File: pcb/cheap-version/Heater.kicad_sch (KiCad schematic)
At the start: 8 parts, among them J601 PTC + / switched - (3.5 mm), Q601 NTMFS5C628NLT1G, U601 UCC27524ADR

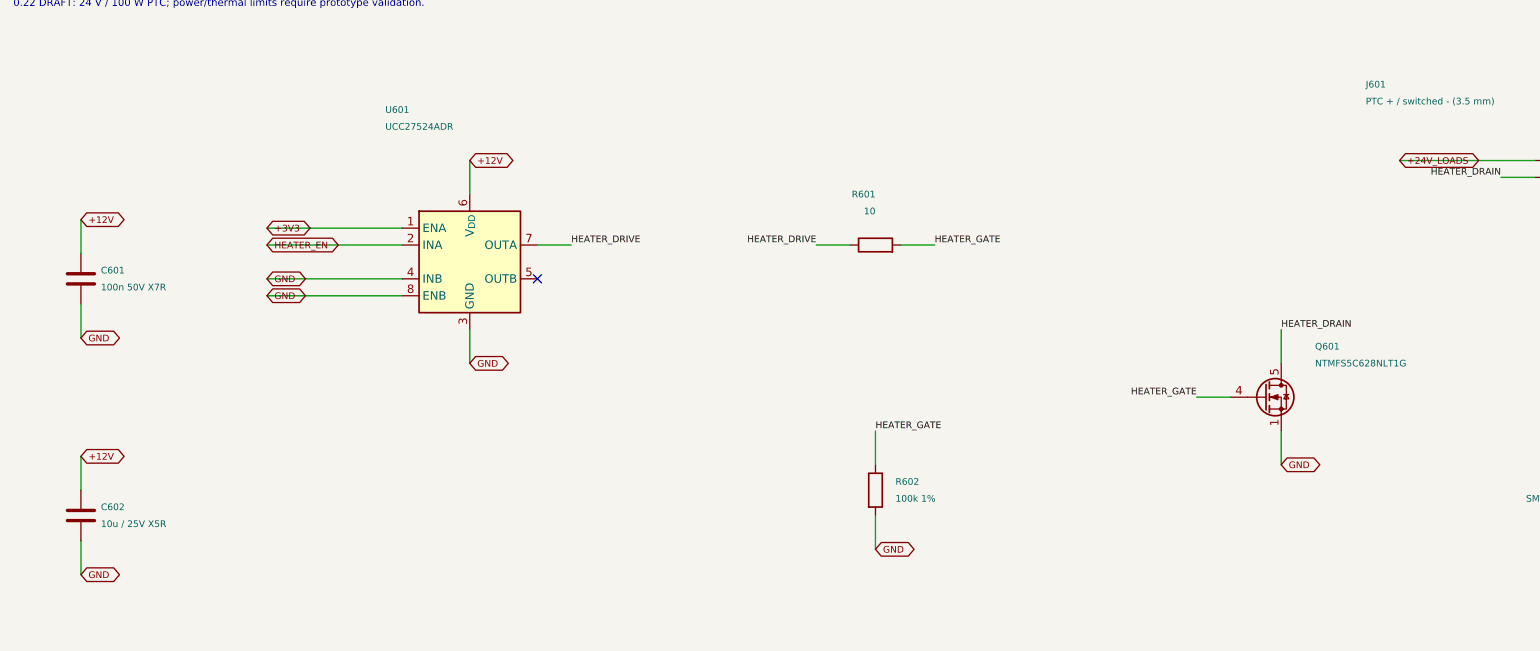
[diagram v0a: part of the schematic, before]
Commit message: cheap-version: schematic substitutions from stock parts
tools/make_cheap1.py generates the cheap-1 sheets from the PCB_V1 0.22 baseline:
ST1S14 for LMR16020 (RT resistor removed, EN/FB divider recalculated), IRS4427S and
IRL2505 for the heater, BSC146N10LS5 for the LED boost switches, SS56 diodes,
KF301/FS1.5/KF2510/XH connectors, stock resistors and capacitors (Source field =
stock:<id>). J901 XT60 is replaced by a screw terminal as decided. U101 TPS54202 and
D711/D721 SS5P10 are kept because datasheets for ST1S10 and SBRT15U100SP5 were not
available. ERC: 0 errors (one warning: footprint for the DTMSS-27 inductor pending);
netdiff against PCB_V1: no connectivity differences among untouched pins.

Co-Authored-By: Claude Sonnet 5.5 <noreply@anthropic.com>
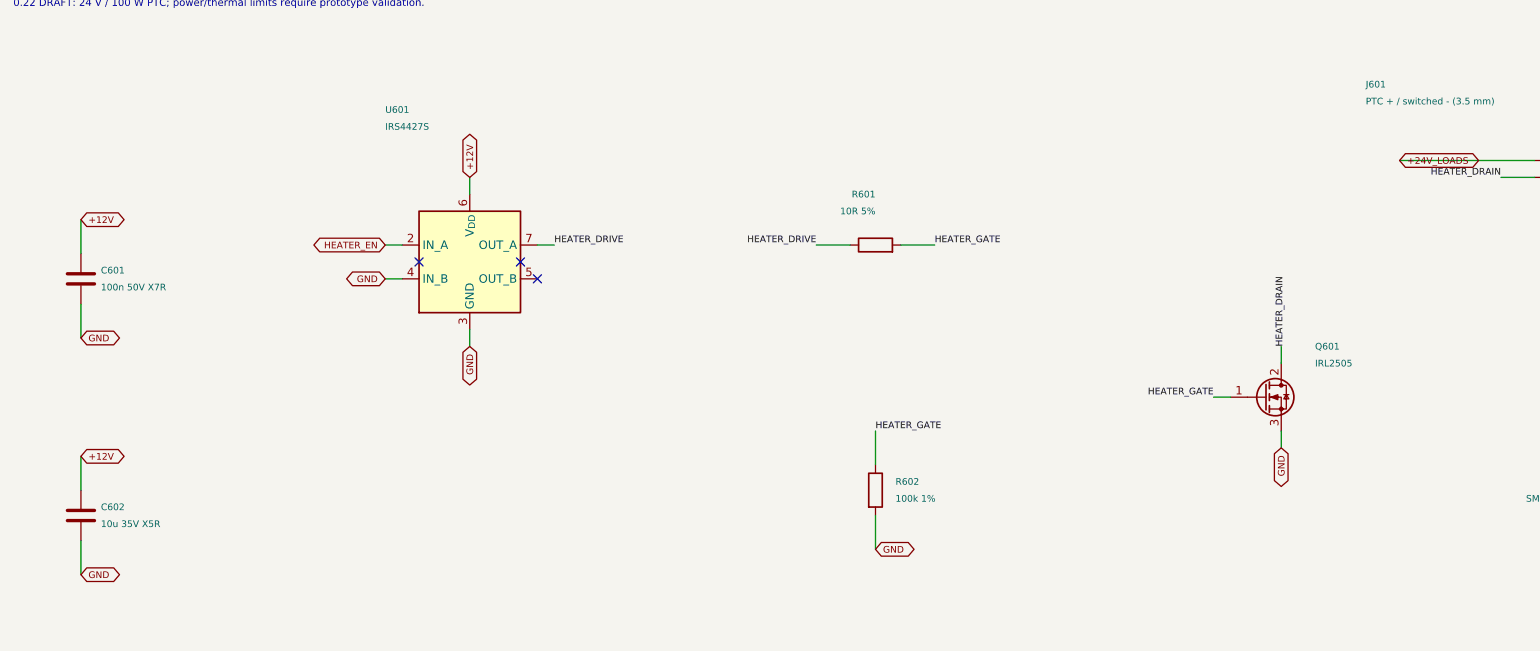
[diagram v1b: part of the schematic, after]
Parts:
- removed Q601: NTMFS5C628NLT1G, Package_SO:ONSemi_SO-8FL_488AA, symbol GrowBox:NTMFS5C628NL
- removed U601: UCC27524ADR, Package_SO:SOIC-8_3.9x4.9mm_P1.27mm, symbol Driver_FET:UCC27524D
- added Q601: IRL2505, Package_TO_SOT_THT:TO-220-3_Vertical, symbol Transistor_FET:Q_NMOS_GDS
- added U601: IRS4427S, Package_SO:SOIC-8_3.9x4.9mm_P1.27mm, symbol Driver_FET:TC4427xOA
- C601: Source (none) -> stock:54
- C602: value 10u / 25V X5R -> 10u 35V X5R; footprint Capacitor_SMD:C_0805_2012Metric -> Capacitor_SMD:C_1210_3225Metric; LCSC C15850 -> C2980162; MPN CL21A106KAYNNNE -> CL32A106KLULNNE; Source (none) -> stock:6
- J601: footprint GrowBox:TerminalBlock_DORABO_DB125-3.5_1x02_P3.50mm_Horizontal -> TerminalBlock_Phoenix:TerminalBlock_Phoenix_PT-1,5-2-3.5-H_1x02_P3.50mm_Horizontal; LCSC C466970 -> (none); MPN DB125-3.5-2P-GN-S -> FS1.5-02-350-2601R; Manufacturer DORABO -> (none); Source (none) -> stock:86
- R601: value 10 -> 10R 5%; footprint Resistor_SMD:R_0603_1608Metric -> Resistor_SMD:R_1206_3216Metric; Source (none) -> stock:41
- R602: LCSC C25803 -> C14675; MPN 0603WAF1003T5E -> RC0603FR-07100KL; Manufacturer UNI-ROYAL -> Yageo; Source (none) -> stock:55
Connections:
- net +12V: now also U601.6 (V_{DD})
- net GND: now also Q601.3 (S), U601.3 (GND), U601.4 (IN_B)
- net HEATER_DRAIN: now also Q601.2 (D)
- net HEATER_DRIVE: now also U601.7 (OUT_A)
- net HEATER_EN: now also U601.2 (IN_A)
- net HEATER_GATE: now also Q601.1 (G)
- no-connect marks 1 -> 3

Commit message: cheap-version: CH1 for 80 W and UCC27524 heater driver
R716 0.18 -> 0.12 ohm (1.667 A, 80 W at 48 V; the LED panel is rated up to
120 W and is not fully loaded). analyze_led_cheap.py re-run: input current
up to 4.61 A, inductor peak 6.26 A, OCP headroom 2.06 A, all model checks
pass; about 96 W is the ceiling of this controller/inductor pair.

U601 is the PCB_V1 UCC27524ADR again instead of the IRS4427S (2.5 V input
threshold left 0.14 V of margin at ESP32 VOH): ENA tied to +12V, ENB to
GND. Board side in tools/swap_heater_driver.py; generator, BOM and BUY
lists follow (order estimate USD 34.69). Schematic ERC 0, schematic and
board match pin by pin.

Co-Authored-By: Claude Sonnet 5.5 <noreply@anthropic.com>
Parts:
- U601: value IRS4427S -> UCC27524ADR; symbol Driver_FET:TC4427xOA -> Driver_FET:UCC27524D; LCSC (none) -> C185857; MPN IRS4427STRPBF -> UCC27524ADR; Manufacturer Infineon -> TI; Source stock:11 -> buy
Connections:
- net +12V: now also U601.1 (ENA)
- net GND: now also U601.8 (ENB)
- no-connect marks 3 -> 1
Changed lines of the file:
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@@
 	)
 	(symbol
-		(lib_id "Driver_FET:TC4427xOA")
+		(lib_id "Driver_FET:UCC27524D")
 		(at 88.9 63.5 0)
 		(unit 1)
@@
 			)
 		)
-		(property "Value" "IRS4427S"
+		(property "Value" "UCC27524ADR"
 			(at 76.2 43.18 0)
 			(effects
@@
 			)
 		)
-		(property "Datasheet" ""
-			(at 88.9 63.5 0)
-			(effects
-				(font
-					(size 1 1)
-				)
-				(hide yes)
-				(justify left)
-			)
-		)
-		(property "Manufacturer" "Infineon"
-			(at 88.9 63.5 0)
-			(effects
-				(font
-					(size 1 1)
-				)
-				(hide yes)
-				(justify left)
-			)
-		)
-		(property "MPN" "IRS4427STRPBF"
-			(at 88.9 63.5 0)
-			(effects
-				(font
-					(size 1 1)
-				)
-				(hide yes)
-				(justify left)
-			)
-		)
-		(property "LCSC" ""
-			(at 88.9 63.5 0)
-			(effects
-				(font
-					(size 1 1)
-				)
-				(hide yes)
-				(justify left)
-			)
-		)
-		(property "Source" "stock:11"
+		(property "Datasheet" "https://www.ti.com/lit/ds/symlink/ucc27524a.pdf"
+			(at 88.9 63.5 0)
+			(effects
+				(font
+					(size 1 1)
+				)
+				(hide yes)
+				(justify left)
+			)
+		)
+		(property "Manufacturer" "TI"
+			(at 88.9 63.5 0)
+			(effects
+				(font
+					(size 1 1)
+				)
+				(hide yes)
+				(justify left)
+			)
+		)
+		(property "MPN" "UCC27524ADR"
+			(at 88.9 63.5 0)
+			(effects
+				(font
+					(size 1 1)
+				)
+				(hide yes)
+				(justify left)
+			)
+		)
+		(property "LCSC" "C185857"
+			(at 88.9 63.5 0)
+			(effects
+				(font
+					(size 1 1)
+				)
+				(hide yes)
+				(justify left)
+			)
+		)
+		(property "Source" "buy"
 			(at 88.9 63.5 0)
 			(effects
@@
 		)
 	)
-	(no_connect
-		(at 81.28 63.5)
+	(wire
+		(pts
+			(xy 78.74 58.42) (xy 76.2 58.42)
+		)
+		(stroke
+			(width 0)
+			(type default)
+		)
+	)
+	(global_label "+12V"
+		(shape bidirectional)
+		(at 76.2 58.42 180)
+		(effects
+			(font
+				(size 1.0 1.0)
+			)
+			(justify right)
+		)
 	)
 	(wire
@@
 		)
 	)
-	(no_connect
-		(at 96.52 63.5)
+	(wire
+		(pts
+			(xy 78.74 68.58) (xy 76.2 68.58)
+		)
+		(stroke
+			(width 0)
+			(type default)
+		)
+	)
+	(global_label "GND"
+		(shape bidirectional)
+		(at 76.2 68.58 180)
+		(effects
+			(font
+				(size 1.0 1.0)
+			)
+			(justify right)
+		)
 	)
 	(symbol
